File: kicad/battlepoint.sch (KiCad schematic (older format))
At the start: 21 parts, among them J1 BTNS, J2 TMR_LEDS, J3 CAP_LEDS, P13 BTNS_IN, P14 OLED_OUT, P17 BTNS_OUT, P5 SPK, P8 AUDIO_JACK, SW1 BTN_UP, SW2 BTN_DWN, SW3 BTN_SEL, U1 DFPLAYER_MINI

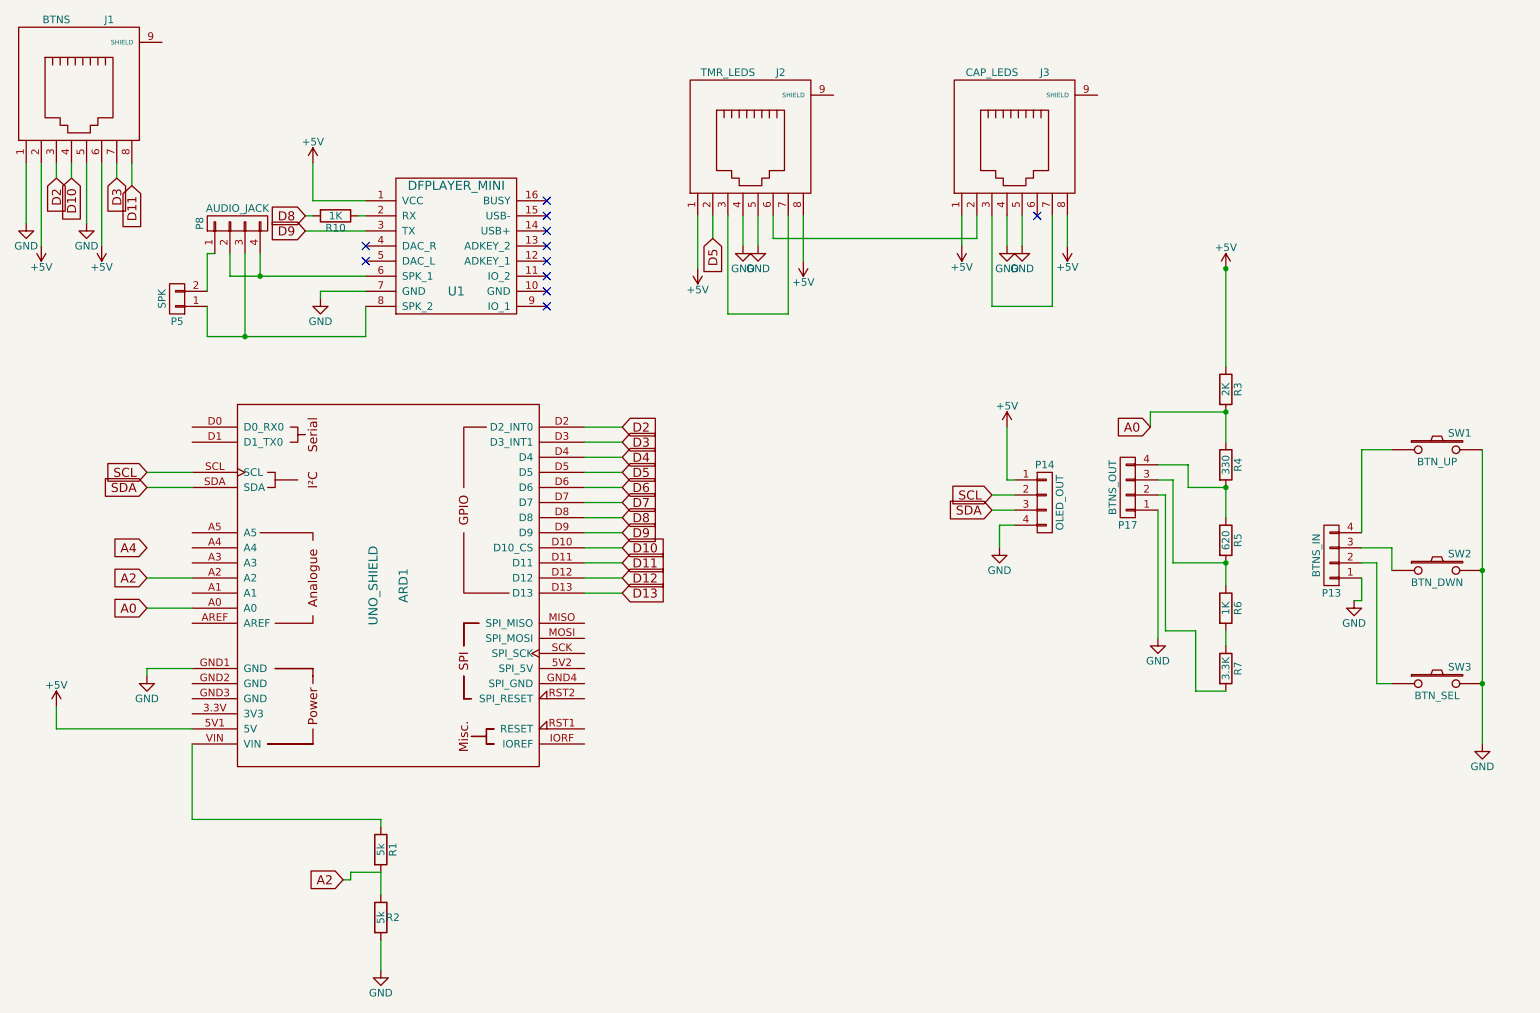
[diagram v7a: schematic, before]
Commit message: add regulator circuit
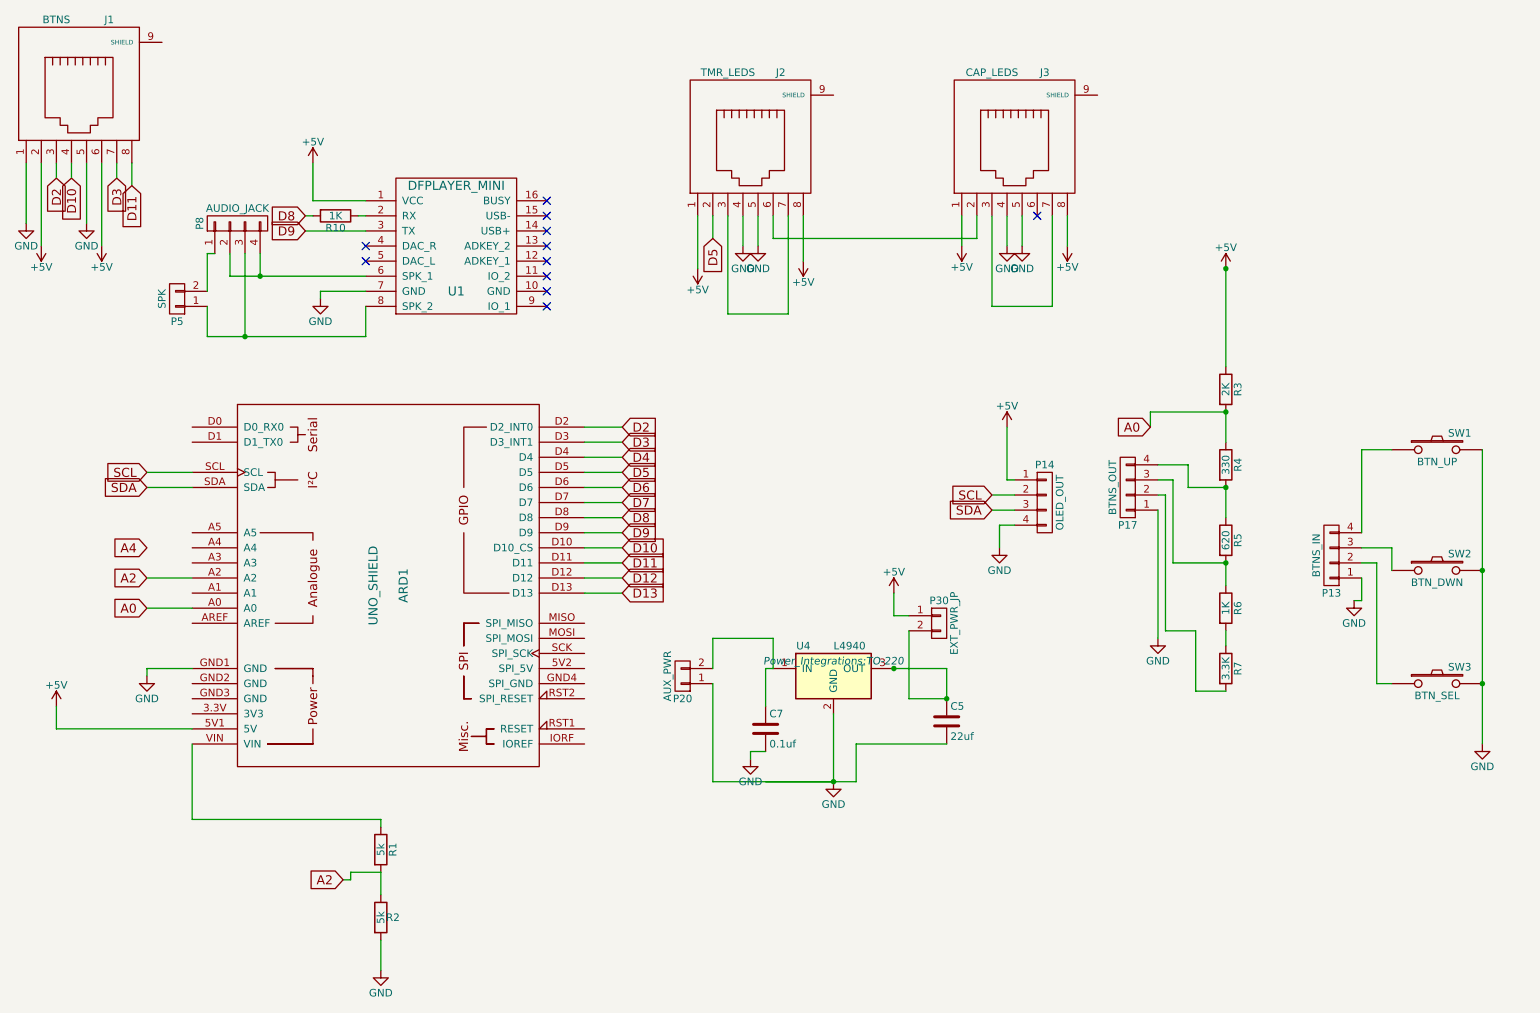
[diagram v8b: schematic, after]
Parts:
- added C5: 22uf, Capacitors_ThroughHole:C_Radial_D7.5_L11.2_P2.5, symbol C
- added C7: 0.1uf, Capacitors_ThroughHole:C_Rect_L4_W2.5_P2.5, symbol C
- added P20: AUX_PWR, Terminal_Blocks:TerminalBlock_Pheonix_MPT-2.54mm_2pol, symbol CONN_01X02
- added P30: EXT_PWR_JP, Pin_Headers:Pin_Header_Straight_1x02, symbol CONN_01X02
- added U4: L4940, Power_Integrations:TO-220, symbol LM7805CT
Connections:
- net +5V: now also P30.1 (P1)
- net GND: now also C5.2, C7.2, P20.1 (P1), U4.2 (GND)
- new net: C7.1, P20.2 (P2), U4.1 (IN)
- new net: C5.1, P30.2 (P2), U4.3 (OUT)
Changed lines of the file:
@@
 	4500 4400 4750 4400
 Wire Wire Line
-	3050 2500 3050 2700
-Wire Wire Line
-	3050 2700 2000 2700
+	3050 2700 3050 2500
+Wire Wire Line
+	2000 2700 3050 2700
 Wire Wire Line
 	2000 2700 2000 2500
@@
 	1600 3700 1900 3700
 Wire Wire Line
-	3050 2300 2150 2300
+	2150 2300 3050 2300
 Wire Wire Line
 	2150 2300 2150 2150
@@
 Wire Wire Line
 	1600 4300 1900 4300
+$Comp
+L LM7805CT U4
+U 1 1 5A3497DA
+P 6150 4950
+F 0 "U4" H 5950 5150 50  0000 C CNN
+F 1 "L4940" H 6150 5150 50  0000 L CNN
+F 2 "Power_Integrations:TO-220" H 6150 5050 50  0000 C CIN
+F 3 "" H 6150 4950 50  0000 C CNN
+	1    6150 4950
+	1    0    0    -1
+$EndComp
+$Comp
+L C C5
+U 1 1 5A3498C1
+P 6900 5250
+F 0 "C5" H 6925 5350 50  0000 L CNN
+F 1 "22uf" H 6925 5150 50  0000 L CNN
+F 2 "Capacitors_ThroughHole:C_Radial_D7.5_L11.2_P2.5" H 6938 5100 50  0001 C CNN
+F 3 "" H 6900 5250 50  0000 C CNN
+	1    6900 5250
+	1    0    0    -1
+$EndComp
+$Comp
+L CONN_01X02 P20
+U 1 1 5A349E9A
+P 5150 4950
+F 0 "P20" H 5150 5100 50  0000 C CNN
+F 1 "AUX_PWR" V 5250 4950 50  0000 C CNN
+F 2 "Terminal_Blocks:TerminalBlock_Pheonix_MPT-2.54mm_2pol" H 5150 4950 50  0001 C CNN
+F 3 "" H 5150 4950 50  0000 C CNN
+	1    5150 4950
+	-1   0    0    1
+$EndComp
+$Comp
+L +5V #PWR024
+U 1 1 5A349FFE
+P 6550 4400
+F 0 "#PWR024" H 6550 4250 50  0001 C CNN
+F 1 "+5V" H 6550 4540 50  0000 C CNN
+F 2 "" H 6550 4400 50  0000 C CNN
+F 3 "" H 6550 4400 50  0000 C CNN
+	1    6550 4400
+	1    0    0    -1
+$EndComp
+$Comp
+L GND #PWR025
+U 1 1 5A34A05D
+P 6150 5650
+F 0 "#PWR025" H 6150 5400 50  0001 C CNN
+F 1 "GND" H 6150 5500 50  0000 C CNN
+F 2 "" H 6150 5650 50  0000 C CNN
+F 3 "" H 6150 5650 50  0000 C CNN
+	1    6150 5650
+	1    0    0    -1
+$EndComp
+Connection ~ 6150 5650
+Wire Wire Line
+	6150 5650 6150 5200
+Wire Wire Line
+	6900 5400 6300 5400
+Wire Wire Line
+	6300 5400 6300 5650
+Wire Wire Line
+	6300 5650 5700 5650
+Wire Wire Line
+	5350 5000 5350 5650
+Wire Wire Line
+	5350 5650 6150 5650
+Connection ~ 6900 5100
+$Comp
+L CONN_01X02 P30
+U 1 1 5A3511C7
+P 6850 4600
+F 0 "P30" H 6850 4750 50  0000 C CNN
+F 1 "EXT_PWR_JP" V 6950 4600 50  0000 C CNN
+F 2 "Pin_Headers:Pin_Header_Straight_1x02" H 6850 4600 50  0001 C CNN
+F 3 "" H 6850 4600 50  0000 C CNN
+	1    6850 4600
+	1    0    0    -1
+$EndComp
+Wire Wire Line
+	6550 4400 6550 4550
+Wire Wire Line
+	6550 4550 6650 4550
+Wire Wire Line
+	6550 4900 6900 4900
+Connection ~ 6550 4900
+Wire Wire Line
+	6900 4900 6900 5100
+Wire Wire Line
+	6900 5100 6650 5100
+Wire Wire Line
+	6650 5100 6650 4650
+$Comp
+L C C7
+U 1 1 5A3538CC
+P 5700 5300
+F 0 "C7" H 5725 5400 50  0000 L CNN
+F 1 "0.1uf" H 5725 5200 50  0000 L CNN
+F 2 "Capacitors_ThroughHole:C_Rect_L4_W2.5_P2.5" H 5738 5150 50  0001 C CNN
+F 3 "" H 5700 5300 50  0000 C CNN
+	1    5700 5300
+	1    0    0    -1
+$EndComp
+Wire Wire Line
+	5750 4900 5700 4900
+Wire Wire Line
+	5700 4900 5700 5150
+$Comp
+L GND #PWR026
+U 1 1 5A3547E8
+P 5600 5500
+F 0 "#PWR026" H 5600 5250 50  0001 C CNN
+F 1 "GND" H 5600 5350 50  0000 C CNN
+F 2 "" H 5600 5500 50  0000 C CNN
+F 3 "" H 5600 5500 50  0000 C CNN
+	1    5600 5500
+	1    0    0    -1
+$EndComp
+Wire Wire Line
+	5700 5450 5600 5450
+Wire Wire Line
+	5600 5450 5600 5500
+Wire Wire Line
+	5350 4900 5350 4700
+Wire Wire Line
+	5350 4700 5750 4700
+Wire Wire Line
+	5750 4700 5750 4900
 $EndSCHEMATC
